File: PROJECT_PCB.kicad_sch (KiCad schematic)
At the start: 16 parts, among them J1 SS-52400-003, J2 B2B-PH-K-S_LF__SN_, U1 MCP73871

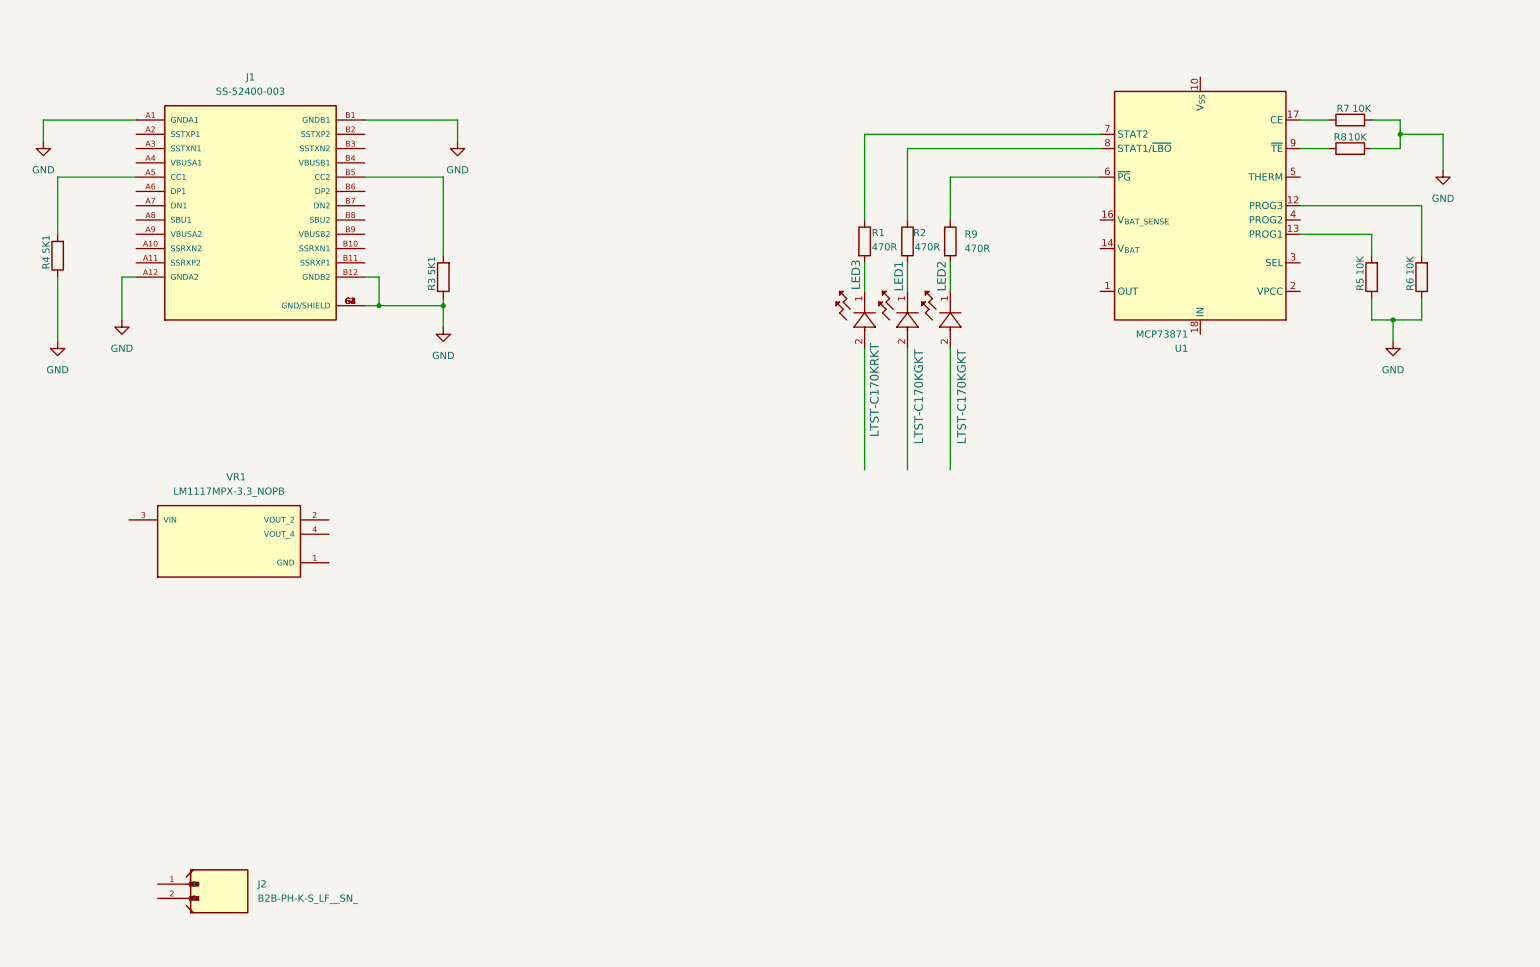
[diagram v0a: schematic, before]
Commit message: schematic additons
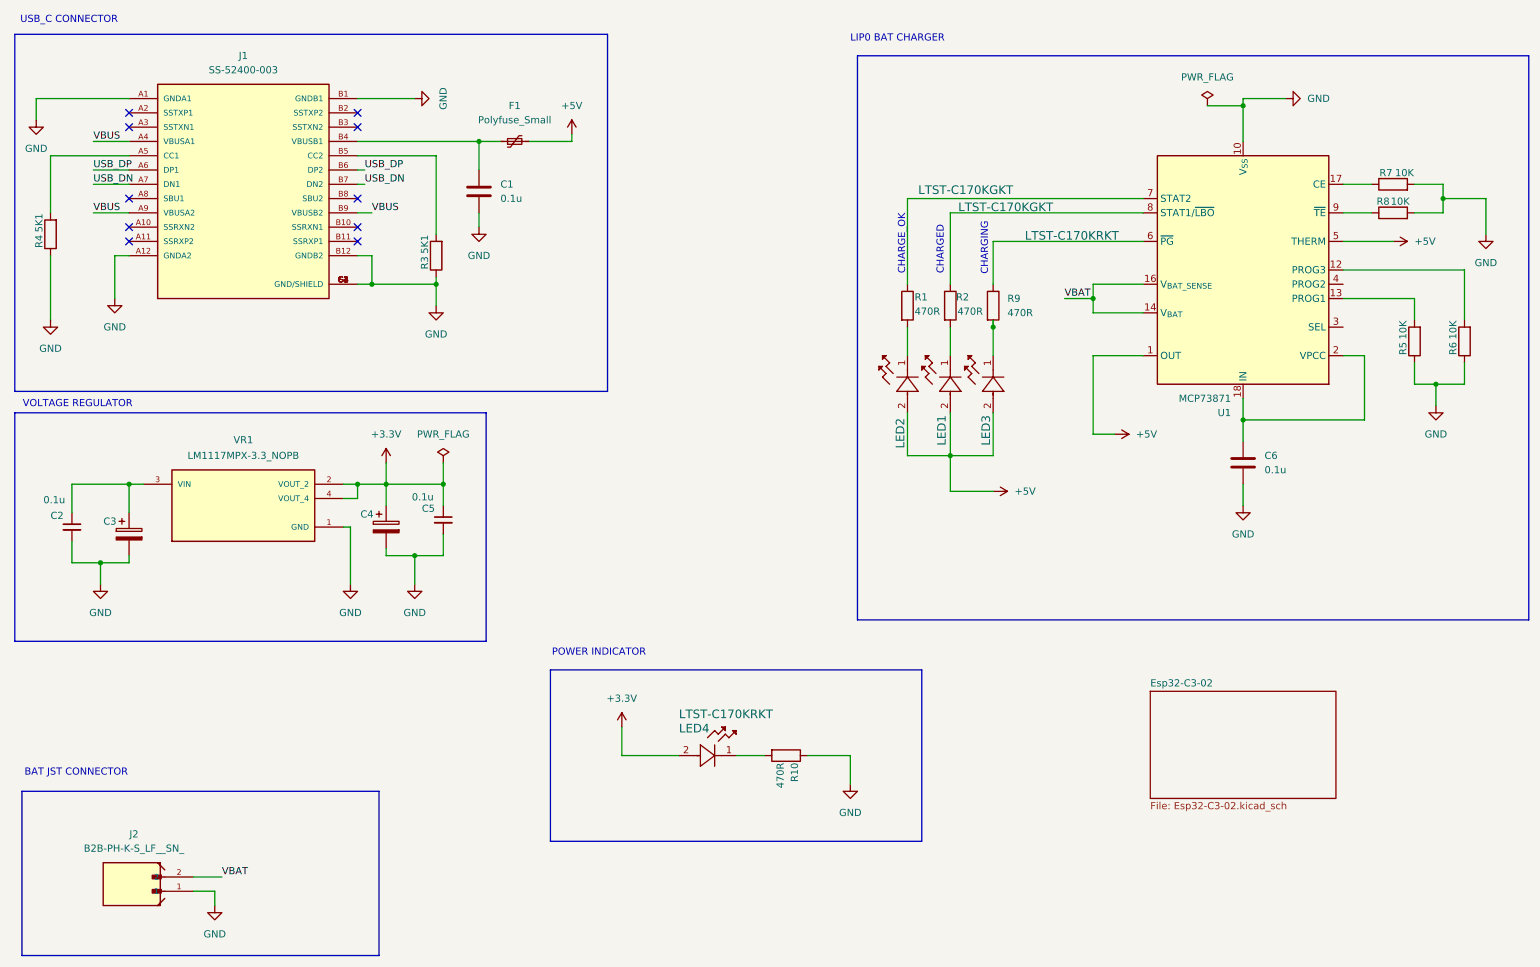
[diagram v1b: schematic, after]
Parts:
- added C1, C6: 0.1u, symbol Device:C
- added C2, C5: 0.1u, symbol Device:C_Small
- added C3, C4: 10u, symbol Device:C_Polarized
- added F1: Polyfuse_Small, symbol Device:Polyfuse_Small
- added LED4: LTST-C170KRKT, LED_LTST-C170KRKT_LTO, symbol 2025-07-01_05-07-46:LTST-C170KRKT
- added R10: 470R, symbol Device:R
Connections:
- net GND: now also J2.1, U1.10 (V_{SS}), U1.11 (V_{SS}), U1.21 (V_{SS}), VR1.1 (GND), C1.2, C2.2, C3.2, C4.2, C5.2, C6.2, R10.1
- net +5V: now reaches LED1.2
- net +5V: now also LED2.2, LED3.2, U1.1 (OUT), U1.20 (OUT), U1.5 (THERM), F1.2
- net VBUS: now reaches J1.A4 (VBUSA1)
- net VBUS: now also J1.A9 (VBUSA2), J1.B9 (VBUSB2)
- net USB_DP: now reaches J1.A6 (DP1)
- net USB_DP: now also J1.B6 (DP2)
- net USB_DN: now reaches J1.A7 (DN1)
- net USB_DN: now also J1.B7 (DN2)
- net at J1.B4 (VBUSB1): now also C1.1, F1.1
- net VBAT: now reaches J2.2
- net VBAT: now also U1.14 (V_{BAT}), U1.15 (V_{BAT}), U1.16 (V_{BAT_SENSE})
- net +3.3V: now reaches VR1.2 (VOUT_2)
- net +3.3V: now also VR1.4 (VOUT_4), C4.1, C5.1, LED4.2
- net at VR1.3 (VIN): now also C2.1, C3.1
- net at U1.18 (IN), U1.19 (IN): now also U1.2 (VPCC), C6.1
- net at R9.2: now also LED3.1; no longer LED2.1
- net at R1.2: now also LED2.1; no longer LED3.1
- new net: LED4.1, R10.2
- no-connect marks 0 -> 10
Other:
- added sheet Esp32-C3-02 (Esp32-C3-02.kicad_sch)
- note added: "BAT JST CONNECTOR"
- note added: "CHARGED"
- note added: "CHARGE_OK"
- note added: "CHARGING"
- note added: "LIP0 BAT CHARGER"
- note added: "POWER INDICATOR"
- note added: "USB_C CONNECTOR"
- note added: "VOLTAGE REGULATOR"
- moved on the sheet: J1, J2, LED1, LED2, LED3, R1, R2, R3, R4, R5, R6, R7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

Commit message: Schematic update
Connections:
- net +5V: now also C2.1, C3.1, VR1.3 (VIN)
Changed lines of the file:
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@@
 	(text "LIP0 BAT CHARGER\n"
 		(exclude_from_sim no)
-		(at 169.672 19.812 0)
+		(at 171.45 19.812 0)
 		(effects
 			(font
@@
 	)
 	(junction
+		(at 22.86 99.06)
+		(diameter 0)
+		(color 0 0 0 0)
+	)
+	(junction
 		(at 265.43 81.28)
 		(diameter 0)
@@
 	(wire
 		(pts
+			(xy 22.86 97.79) (xy 22.86 99.06)
+		)
+		(stroke
+			(width 0)
+			(type default)
+		)
+	)
+	(wire
+		(pts
 			(xy 88.9 95.25) (xy 88.9 99.06)
 		)
@@
 	)
 	(symbol
+		(lib_id "power:+5V")
+		(at 22.86 97.79 0)
+		(unit 1)
+		(exclude_from_sim no)
+		(in_bom yes)
+		(on_board yes)
+		(dnp no)
+		(fields_autoplaced yes)
+		(property "Reference" "#PWR022"
+			(at 22.86 101.6 0)
+			(effects
+				(font
+					(size 1.27 1.27)
+				)
+				(hide yes)
+			)
+		)
+		(property "Value" "+5V"
+			(at 22.86 92.71 0)
+			(effects
+				(font
+					(size 1.27 1.27)
+				)
+			)
+		)
+		(property "Footprint" ""
+			(at 22.86 97.79 0)
+			(effects
+				(font
+					(size 1.27 1.27)
+				)
+				(hide yes)
+			)
+		)
+		(property "Datasheet" ""
+			(at 22.86 97.79 0)
+			(effects
+				(font
+					(size 1.27 1.27)
+				)
+				(hide yes)
+			)
+		)
+		(property "Description" "Power symbol creates a global label with name \"+5V\""
+			(at 22.86 97.79 0)
+			(effects
+				(font
+					(size 1.27 1.27)
+				)
+				(hide yes)
+			)
+		)
+		(pin "1"
+		)
+		(instances
+			(project ""
+				(path "/cd744ce3-b5f7-4fbf-afc5-dbe11b3dff46"
+					(reference "#PWR022")
+					(unit 1)
+				)
+			)
+		)
+	)
+	(symbol
 		(lib_id "Device:C_Polarized")
 		(at 33.02 107.95 0)
@@
 		)
 		(fill
-			(color 0 0 0 0.0000)
+			(color 255 0 2 1.0000)
 		)
 		(property "Sheetname" "Esp32-C3-02"
